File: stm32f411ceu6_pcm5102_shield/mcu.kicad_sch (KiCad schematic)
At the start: 25 parts, among them J100 Conn_01x04_Pin, J101 Conn_01x04_Pin, SW100 RotaryEncoder_Switch_MP, U100 BlackPill, U101 INMP411

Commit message: Initial layout
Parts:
- removed Brd100: SSD1306, stm32f401_pcm5102_shiled_lib:128x64OLED, symbol stm32f401_pcm5102_shiled_lib:SSD1306
- added J102: Conn_01x04_Pin, Connector_PinHeader_2.54mm:PinHeader_1x04_P2.54mm_Vertical, symbol Connector:Conn_01x04_Pin
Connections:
- net +3.3V: now also J102.2 (Pin_2)
- net GND: now also J102.1 (Pin_1)
- net I2C1_SCL: now also J102.3 (Pin_3)
- net I2C1_SDA: now also J102.4 (Pin_4)
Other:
- moved on the sheet: D1, R110, U101

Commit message: First PCB routing
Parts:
- added D101: LED, LED_THT:LED_D3.0mm, symbol Device:LED
- added R111: 1kR, Resistor_SMD:R_0805_2012Metric, symbol Device:R
- renumbered D1 to D100
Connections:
- net +5V: now also U100.20 (5V); no longer U100.23 (5V)
- net GND: now also U100.19 (GND), R111.2
- net LED_SPK_MUTE: now reaches U100.6 (PA0)
- net LED_SPK_MUTE: now also D101.2 (A)
- net at R103.2, R105.1, SW100.A: no longer R102.2, R104.2, SW100.B
- new net: R102.2, R104.2, SW100.B
- new net: D101.1 (K), R111.1
- no-connect marks 19 -> 17

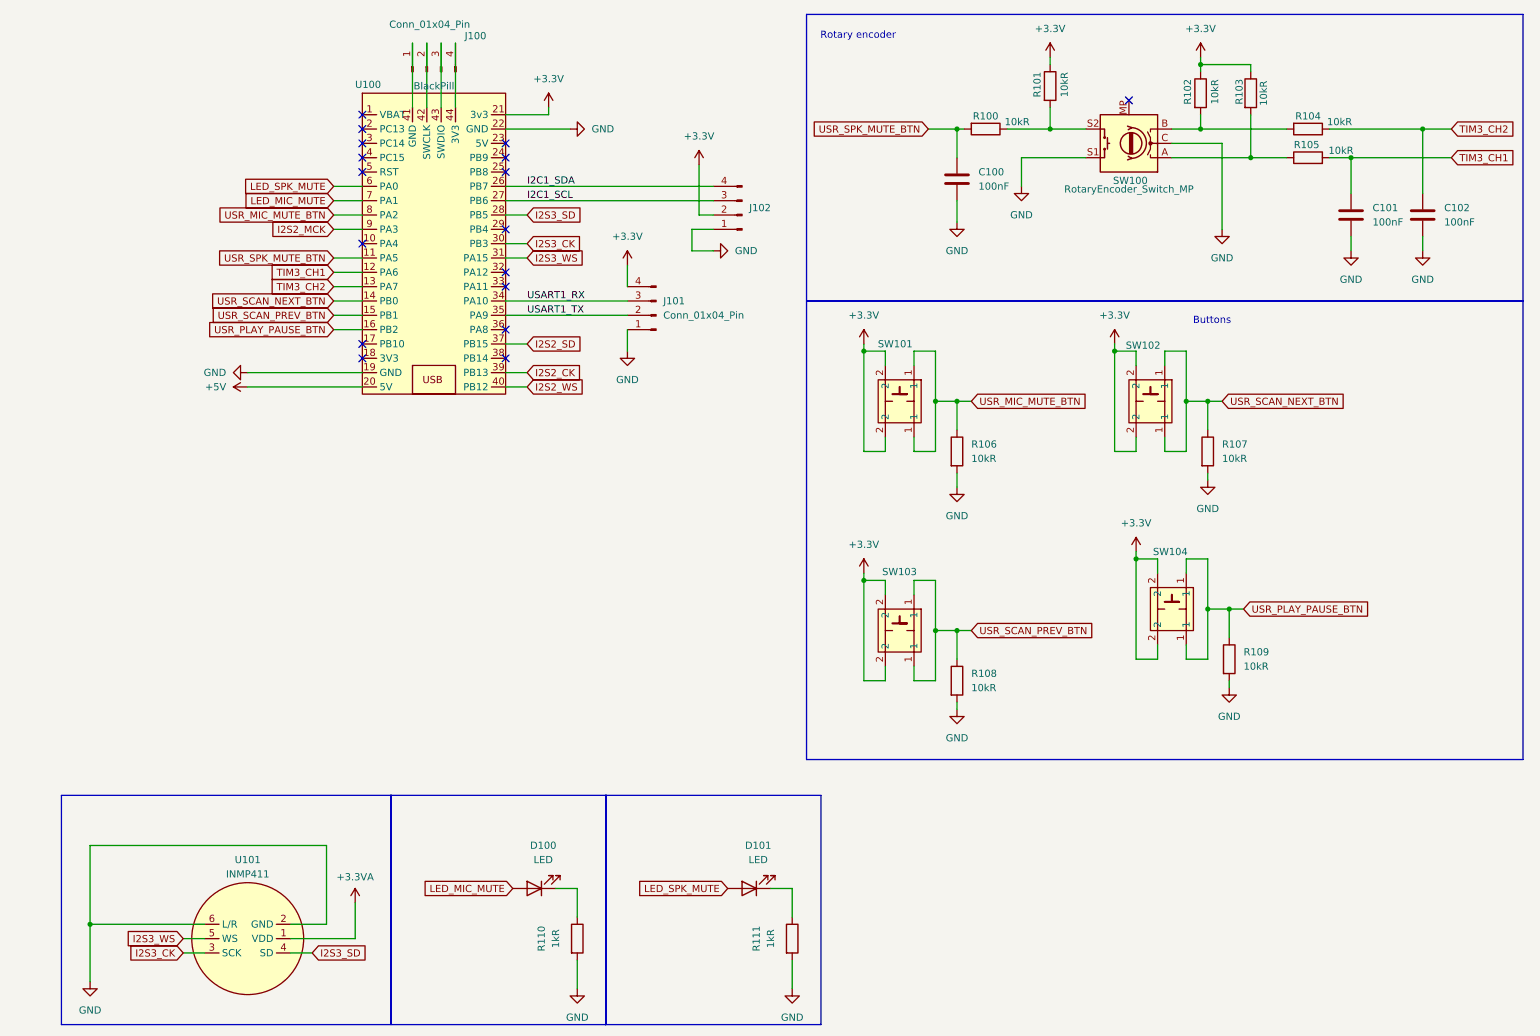
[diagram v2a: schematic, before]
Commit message: Update firmware to simplify routing
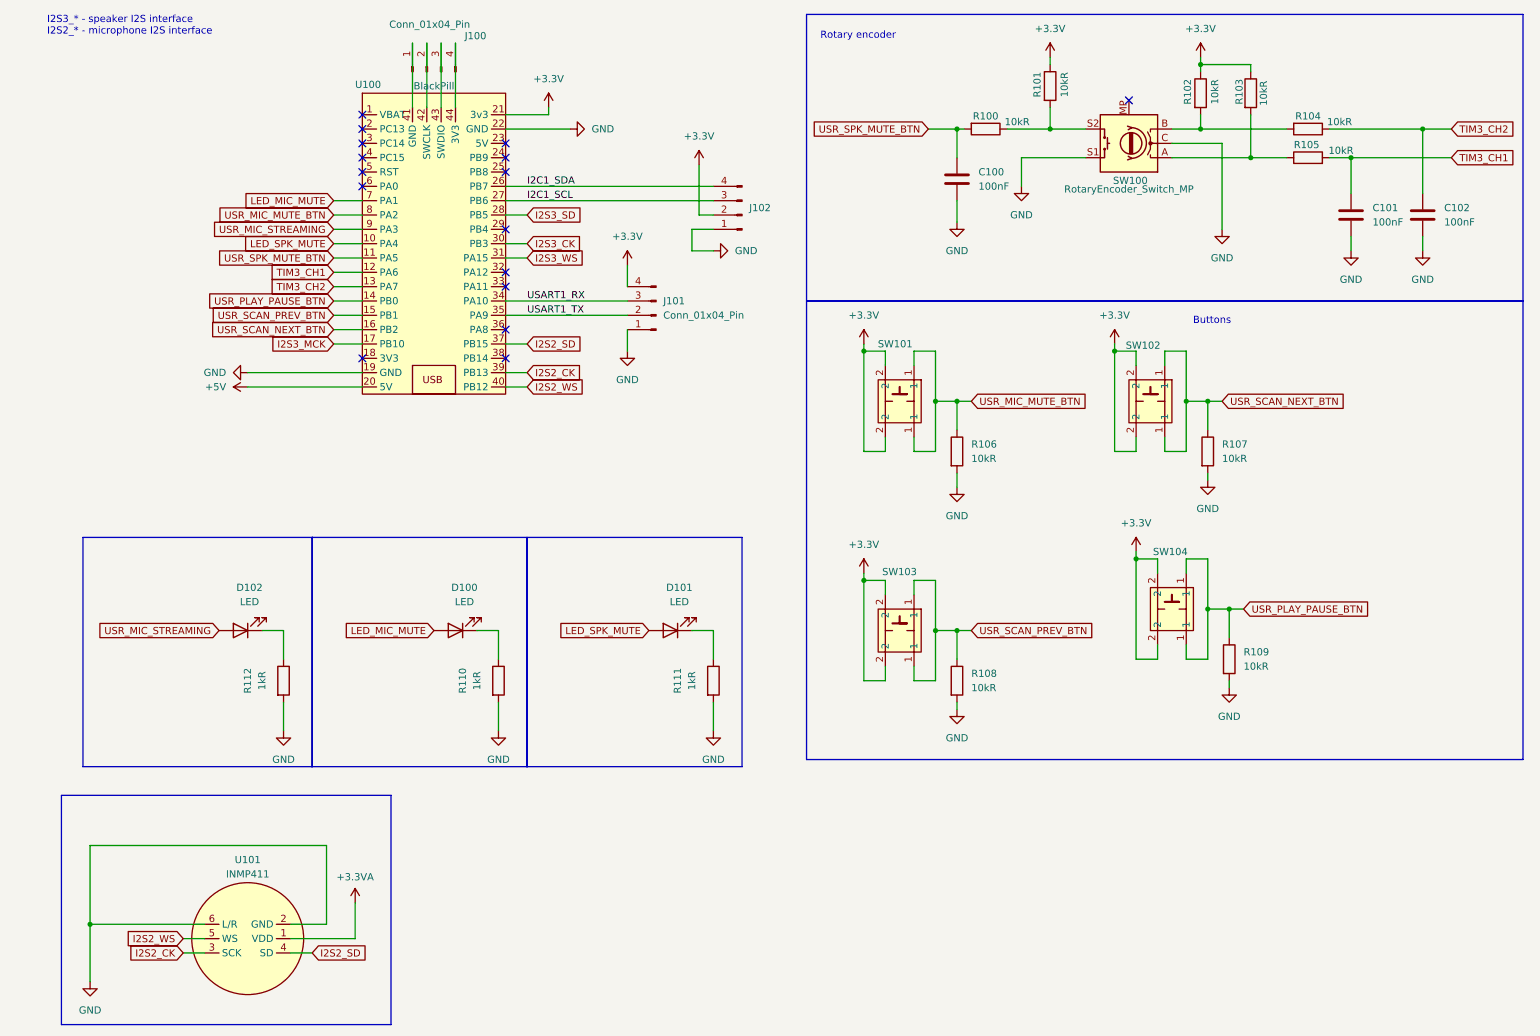
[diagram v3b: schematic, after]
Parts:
- added D102: LED, LED_THT:LED_D3.0mm, symbol Device:LED
- added R112: 1kR, Resistor_SMD:R_0805_2012Metric, symbol Device:R
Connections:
- net GND: now also R112.2
- net I2S2_CK: now also U101.3 (SCK)
- net I2S2_SD: now also U101.4 (SD)
- net I2S2_WS: now also U101.5 (WS)
- net I2S3_CK: no longer U101.3 (SCK)
- net I2S3_SD: no longer U101.4 (SD)
- net I2S3_WS: no longer U101.5 (WS)
- net LED_SPK_MUTE: now also U100.10 (PA4); no longer U100.6 (PA0)
- net USR_PLAY_PAUSE_BTN: now also U100.14 (PB0); no longer U100.16 (PB2)
- net USR_SCAN_NEXT_BTN: now also U100.16 (PB2); no longer U100.14 (PB0)
- net I2S3_MCK: now reaches U100.17 (PB10)
- net I2S2_MCK renamed USR_MIC_STREAMING
- net USR_MIC_STREAMING: now also D102.2 (A)
- new net: D102.1 (K), R112.1
- no-connect marks 17 -> 16
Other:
- note added: "I2S3_* - speaker I2S interface I2S2_* - microphone I2S interface"
- moved on the sheet: D100, D101, R110, R111
